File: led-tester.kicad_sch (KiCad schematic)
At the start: 23 parts, among them M1 Arduino_Mini, U1 PCF8591

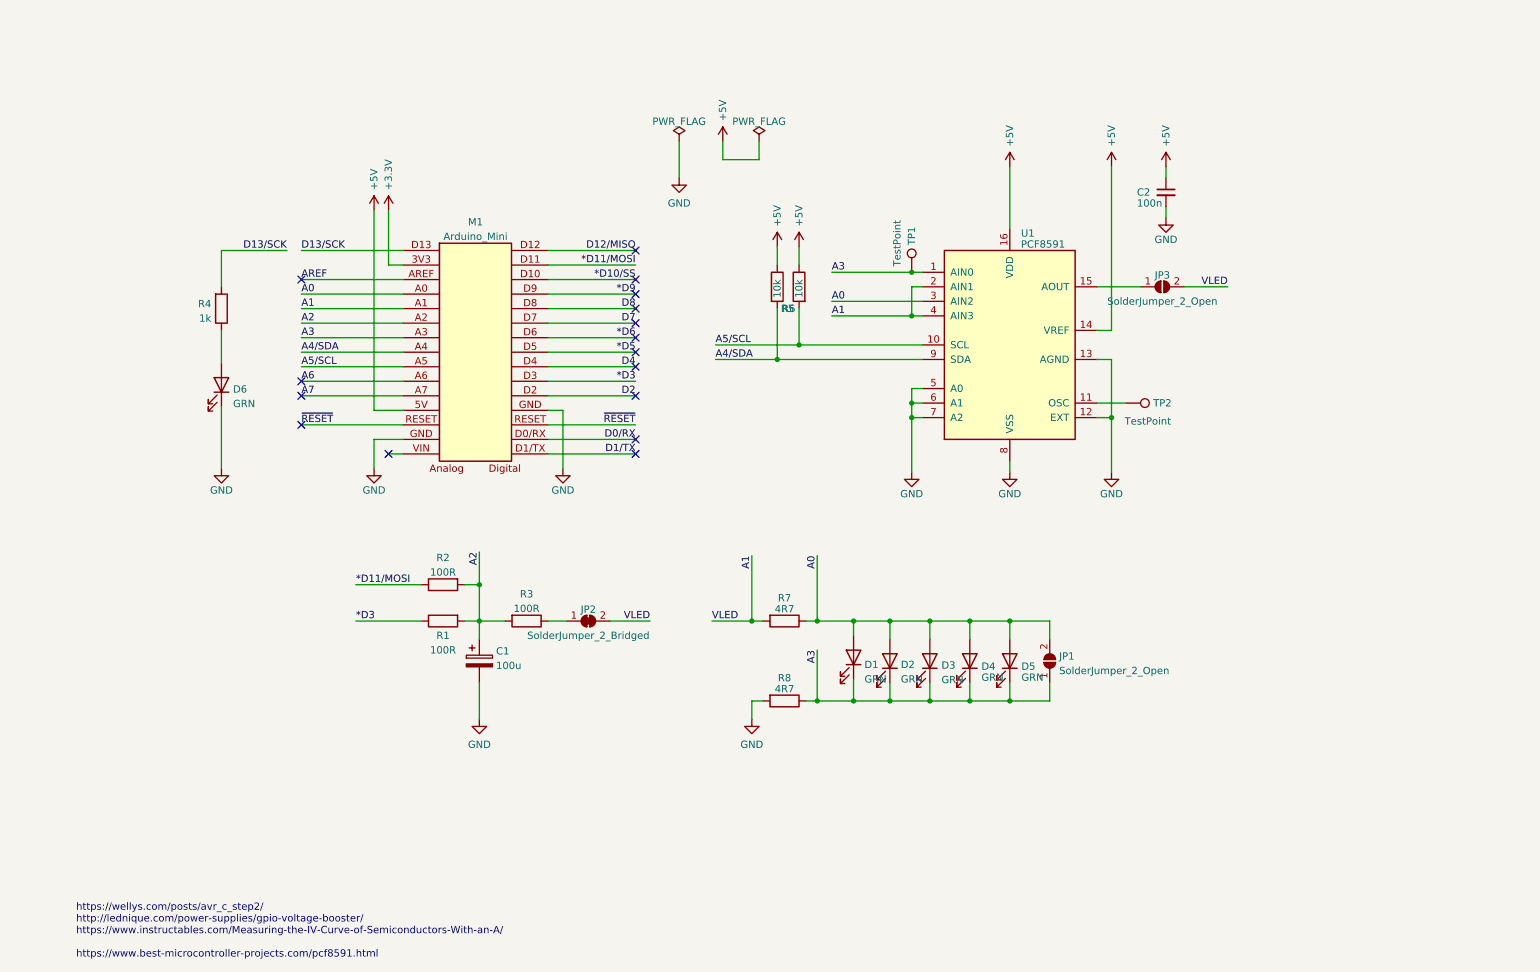
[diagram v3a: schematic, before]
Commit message: Complete redesign to add op-amp buffer, 2-stage LP filter and fit in 5x5cm.
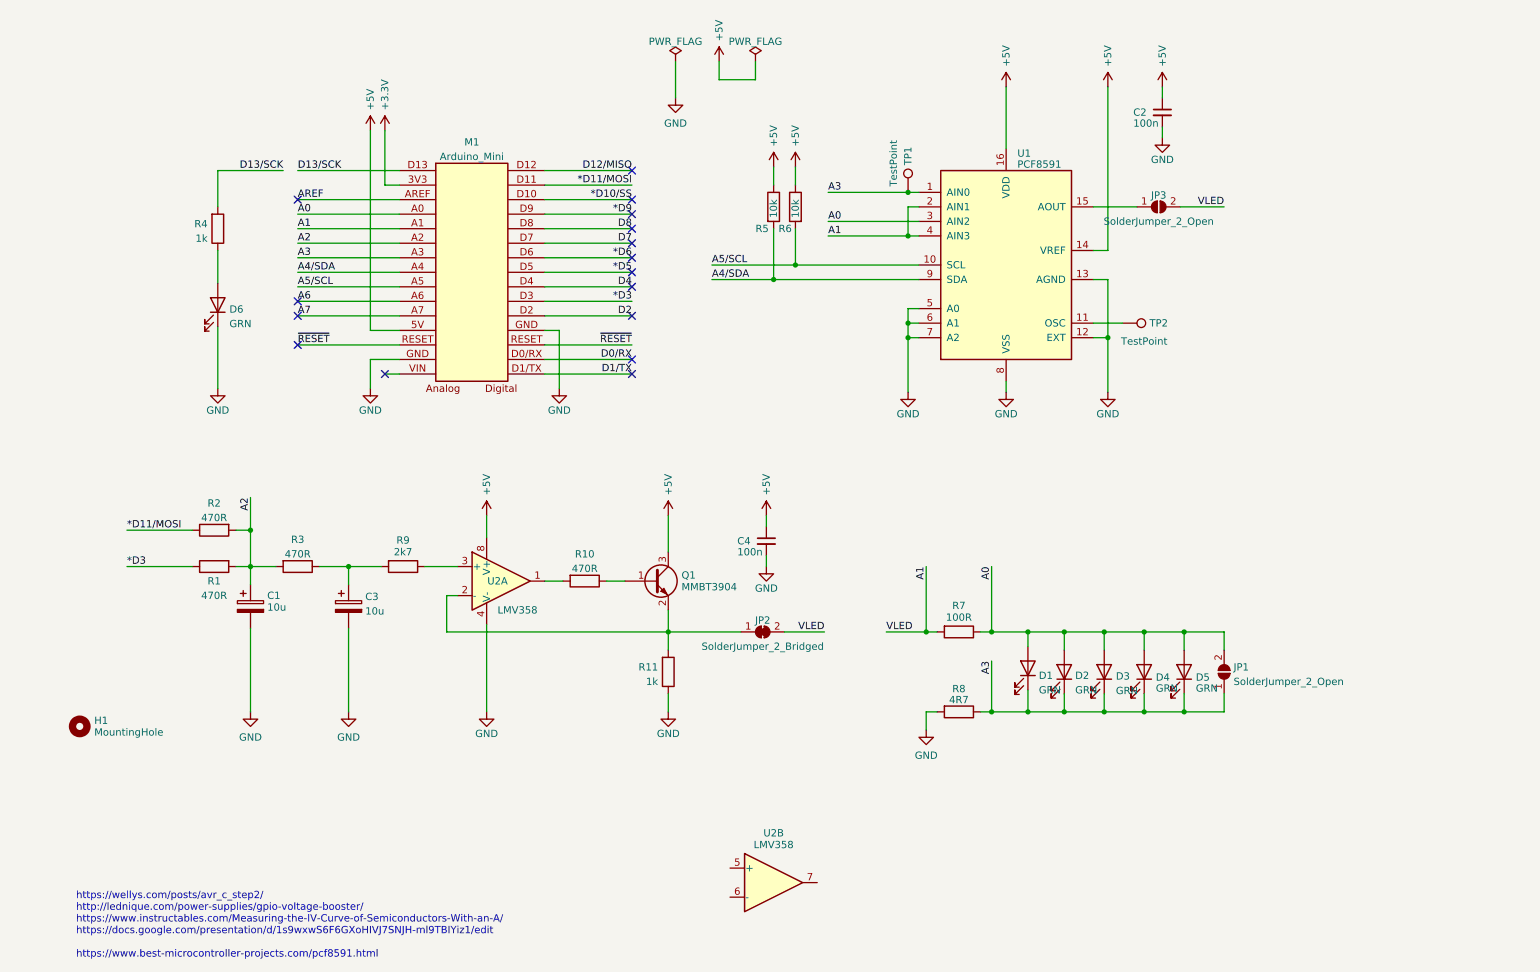
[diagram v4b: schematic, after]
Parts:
- added C3: 10u, Capacitor_THT:CP_Radial_D5.0mm_P2.00mm, symbol Device:C_Polarized
- added C4: 100n, Capacitor_SMD:C_0805_2012Metric_Pad1.18x1.45mm_HandSolder, symbol Device:C_Small
- added H1: MountingHole, aalib:AlignmentSlot, symbol Mechanical:MountingHole
- added Q1: MMBT3904, Package_TO_SOT_SMD:SOT-23, symbol Transistor_BJT:MMBT3904
- added R10: 470R, Resistor_SMD:R_0805_2012Metric_Pad1.20x1.40mm_HandSolder, symbol Device:R
- added R11: 1k, Resistor_SMD:R_0805_2012Metric_Pad1.20x1.40mm_HandSolder, symbol Device:R
- added R9: 2k7, Resistor_SMD:R_0805_2012Metric_Pad1.20x1.40mm_HandSolder, symbol Device:R
- added U2: LMV358, Package_SO:SOIC-8_3.9x4.9mm_P1.27mm, symbol Amplifier_Operational:LMV358
- C1: value 100u -> 10u
- R1, R2, R3: value 100R -> 470R
- R7: value 4R7 -> 100R
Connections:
- net +5V: now also C4.1, Q1.3 (C), U2.8 (V+)
- net GND: now also C3.2, C4.2, R11.1, U2.4 (V-)
- net at R3.1: now also C3.1, R9.2; no longer JP2.1 (A)
- new net: R9.1, U2.3 (+)
- new net: Q1.1 (B), R10.1
- new net: JP2.1 (A), Q1.2 (E), R11.2, U2.2 (-)
- new net: R10.2, U2.1
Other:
- note added: "https://wellys.com/posts/avr_c_step2/ http://lednique.com/power-supplies/gpio-voltage-booster/ https://www.instructables.com/Measuring-the-IV-Curve-of-Semiconductors-With-an-A/ https://docs.google.com/presentation/d/1s9wxwS6F6GXoHIVJ7SNJH-ml9TBIYiz1/edit https://www.best-microcontroller-projects.com/pcf8591.html"
- note removed: "https://wellys.com/posts/avr_c_step2/ http://lednique.com/power-supplies/gpio-voltage-booster/ https://www.instructables.com/Measuring-the-IV-Curve-of-Semiconductors-With-an-A/ https://www.best-microcontroller-projects.com/pcf8591.html"
- moved on the sheet: C1, C2, D1, D2, D3, D4, D5, D6, JP1, JP2, JP3, M1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

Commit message: Added a common-anode RGB LED.
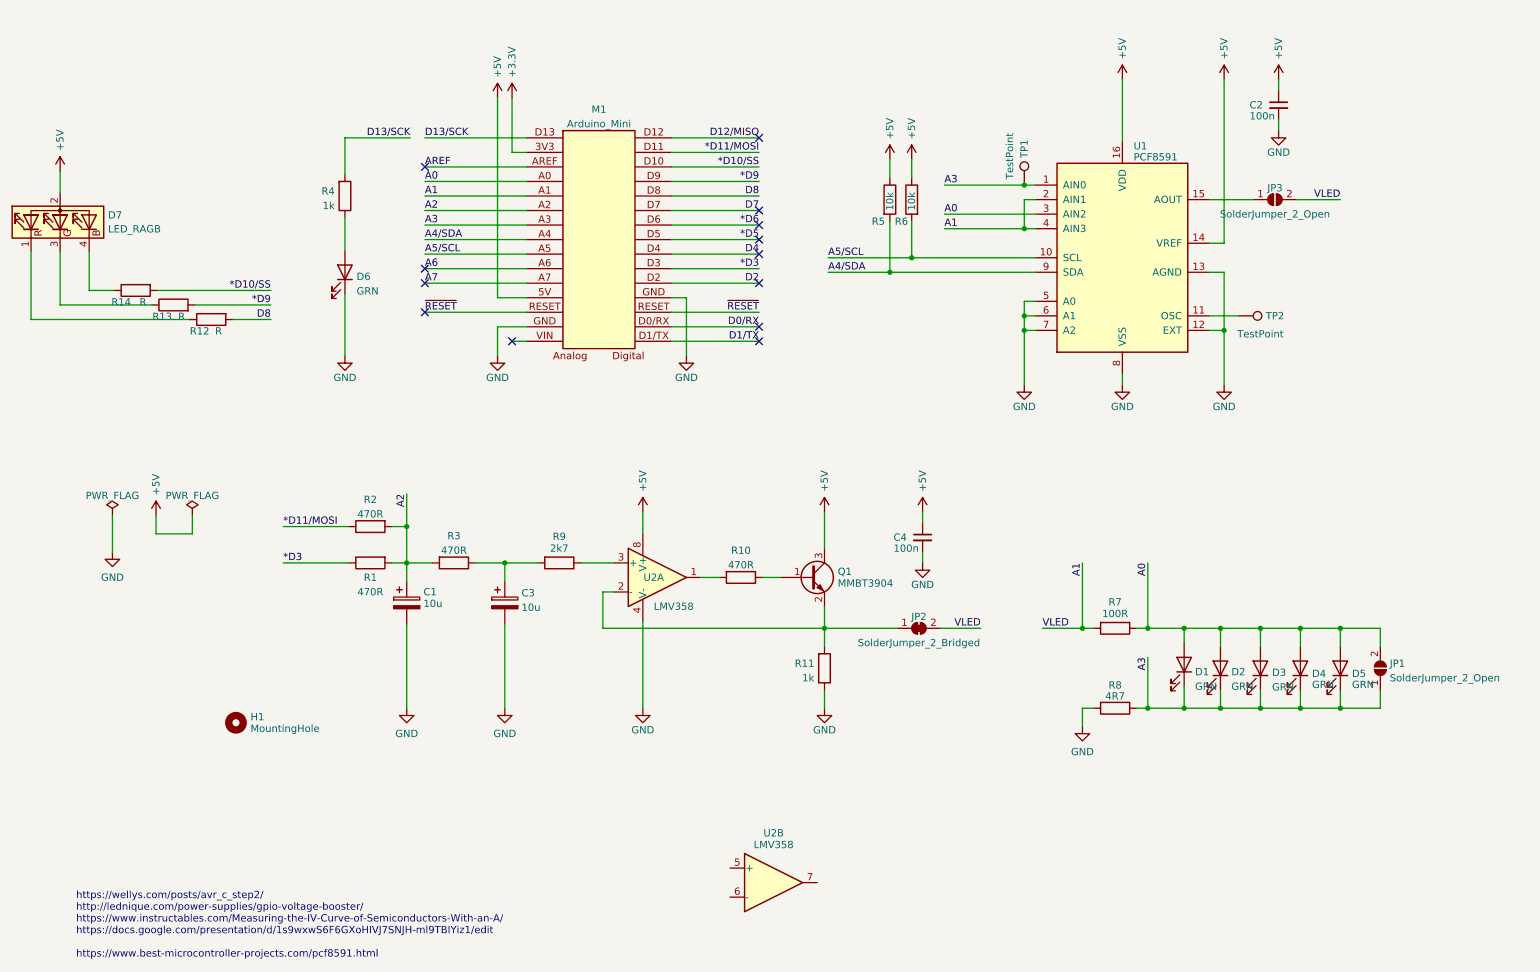
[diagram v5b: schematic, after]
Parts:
- added D7: LED_RAGB, aalib:LED_D8.0mm-4_RGB, symbol Device:LED_RAGB
- added R12, R13, R14: R, Resistor_SMD:R_0603_1608Metric, symbol Device:R
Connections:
- net *D10/SS: now also R14.2
- net *D9: now also R13.2
- net +5V: now also D7.2 (A)
- net D8: now also R12.2
- new net: D7.4 (BK), R14.1
- new net: D7.3 (GK), R13.1
- new net: D7.1 (RK), R12.1
- no-connect marks 16 -> 13
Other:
- moved on the sheet: C1, C2, C3, C4, D1, D2, D3, D4, D5, D6, H1, JP1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
